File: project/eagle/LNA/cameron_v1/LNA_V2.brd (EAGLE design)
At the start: 50 x 45.8 mm, 16 parts, among them Q1 MMBT3906LT1SMD, Q2 MMBT3906LT1SMD, Q3 SAV-541+, X1 SMA-142-0701-871/876, X2 SMA-142-0701-871/876

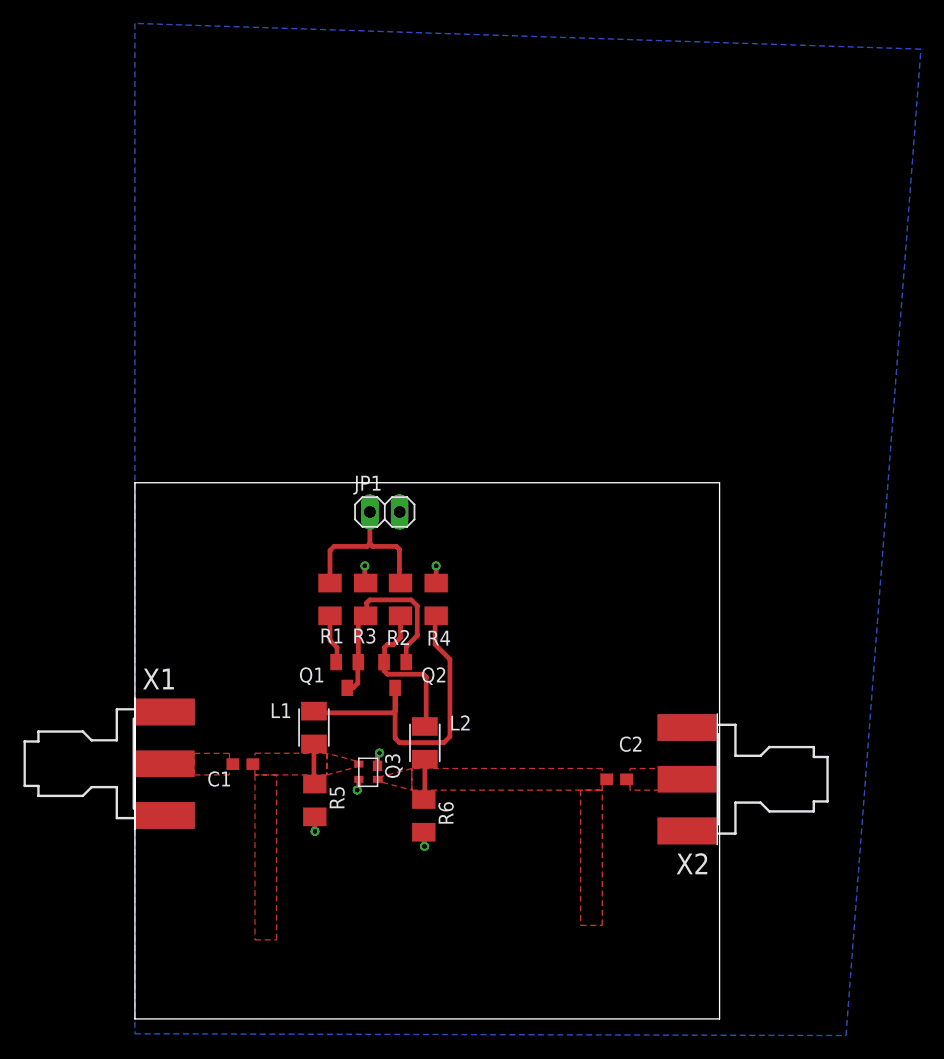
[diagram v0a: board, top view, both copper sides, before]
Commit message: Made version 2 of LNA. Added text and corrected footprints
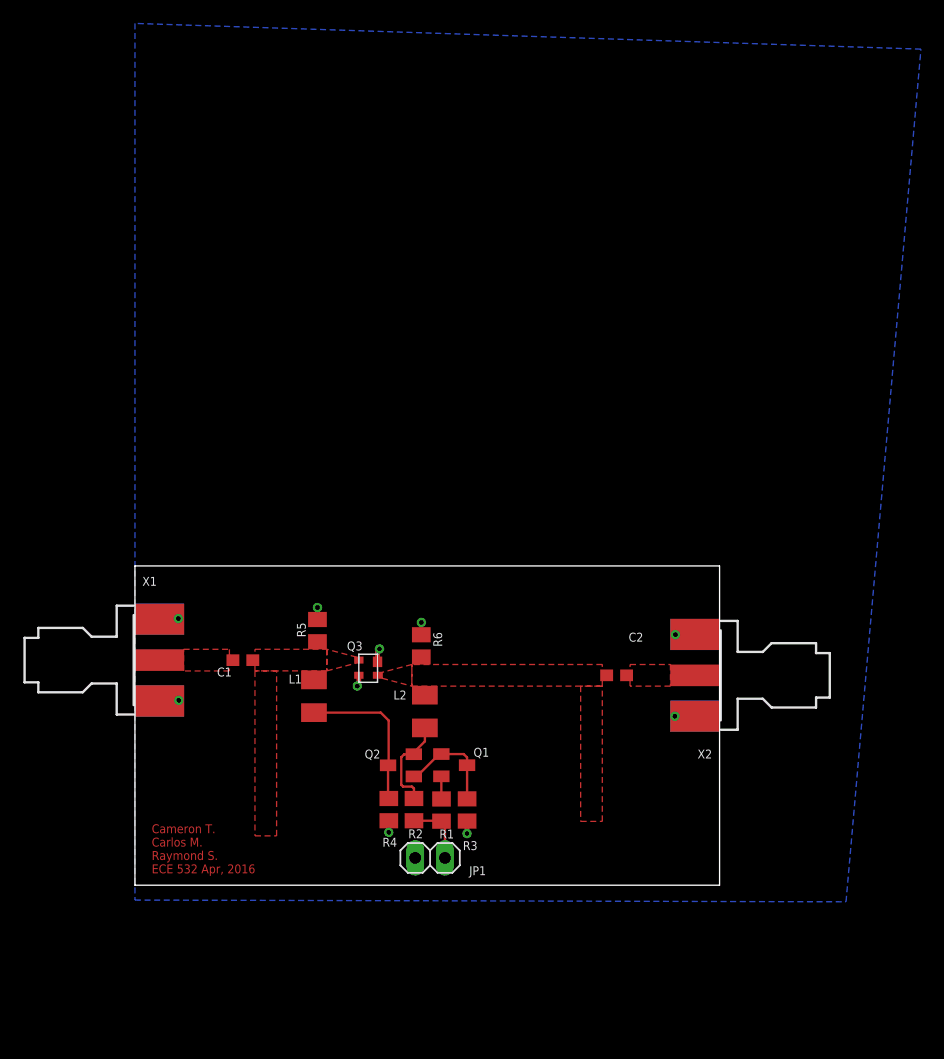
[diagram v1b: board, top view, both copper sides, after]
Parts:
- R1, R2, R3, R4, R5, R6: device rcl:M1206 -> rcl:M0805
- X1, X2: value SMA-142-0701-871/876 -> SMA-142-0711-821/826; device con-coax:J502-ND-142-0701-871/876 -> con-coax:J502-ND-142-0711-821/826
- moved JP1 29.8 mm to (25.2, 2.33), turned to 180 degrees
- moved R1 20.4 mm to (26.2, 6.42), turned to 270 degrees
- moved R3 20.0 mm to (28.4, 6.43), turned to 270 degrees
- moved R4 18.4 mm to (21.7, 6.46), turned to 270 degrees
- moved R2 18.0 mm to (23.8, 6.46), turned to 270 degrees
- moved R6 14.5 mm to (24.5, 20.5), turned to 90 degrees
- moved R5 14.5 mm to (15.6, 21.8), turned to 90 degrees
- moved Q1 12.0 mm to (27.3, 10.3), turned to 270 degrees
- moved C1 8.89 mm to (9.22, 19.2)
- moved C2 8.89 mm to (41.2, 17.9)
- moved Q3 8.89 mm to (19.1, 19.2)
- moved X2 8.88 mm to (50.0, 17.9)
- moved X1 8.86 mm to (-0.01, 19.2)
- moved Q2 7.74 mm to (22.7, 10.2), turned to 90 degrees
- moved L2 2.68 mm to (24.8, 14.8), turned to 90 degrees
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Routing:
- net VG: track 29.3 -> 13.4 mm
- net +3.3V: track 14.8 -> 5.63 mm
- net N$1: track 18.1 -> 9.01 mm
- net VD: track 13.7 -> 8.24 mm
- net INPUT: track 3.49 -> 0.00 mm
- net OUTPUT: track 3.48 -> 0.00 mm
- net N$4: track 4.24 -> 1.94 mm
- net GND: track 7.58 -> 6.28 mm, vias 6 -> 10
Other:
- board size 50 x 45.8 mm -> 50 x 27.3 mm
- board text added: "Cameron T. Carlos M. Raymond S. ECE 532 Apr, 2016"
